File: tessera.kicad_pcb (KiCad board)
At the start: 4 copper layers, 54 x 85.6 mm, 108 parts, among them J1 USB-C, J2 532610271, J3 PinHeader_2x05, Q1 NTK3139P, Q2 NTK3134N, Q3 NTK3134N, SW1 EVQP7A01P, SW2 EVQP7A01P, U1 USBLC6-2P6, U2 BQ25170J, U3 TPS62840DLCR, U4 ISP1807-LR-RS, U5 D3V3XA4B10LP, U6 ST25DV64KC-JF6D3, U7 STSAFA120DFSPL05

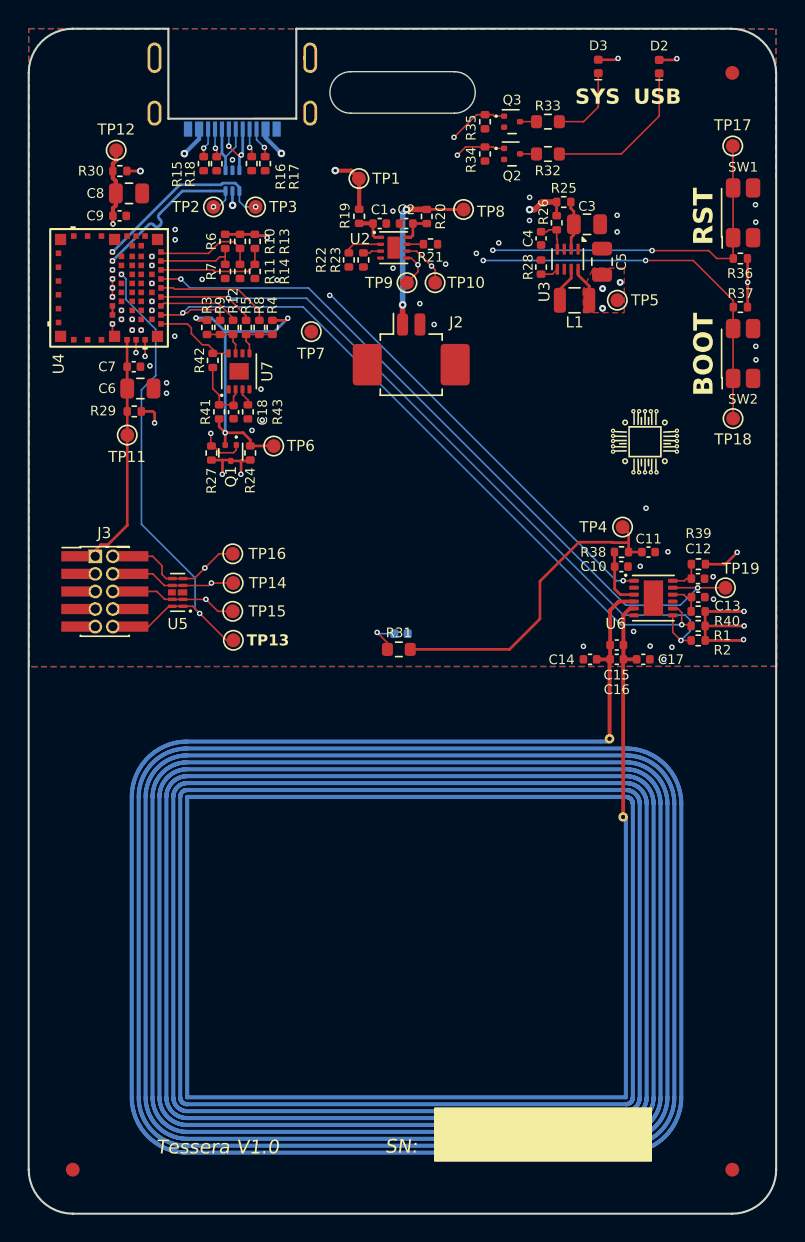
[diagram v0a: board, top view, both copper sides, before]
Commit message: fix(hardware): tighten PCB edge clearance and diff-pair rules, update logo
- Bump lib submodule: assign IPNs to another batch of approved
  capacitor selections
- Update the embedded logo artwork on every schematic sheet to the
  new Logos/logo.png
- Increase min_copper_edge_clearance to 0.5mm and raise net class
  clearance/spacing to match
- Replace the generic outer/inner-layer trace width & spacing rules
  with a dedicated "USB Diff Pair clearance to other nets" rule
  (0.2023mm, excluding intra-pair spacing already governed by the
  netclass diff_pair_gap)
- Add DRC exclusions for pre-existing clearance/copper-edge/solder-
  mask-bridge items surfaced by the tightened edge-clearance rule
- Continue schematic placement and PCB routing/placement
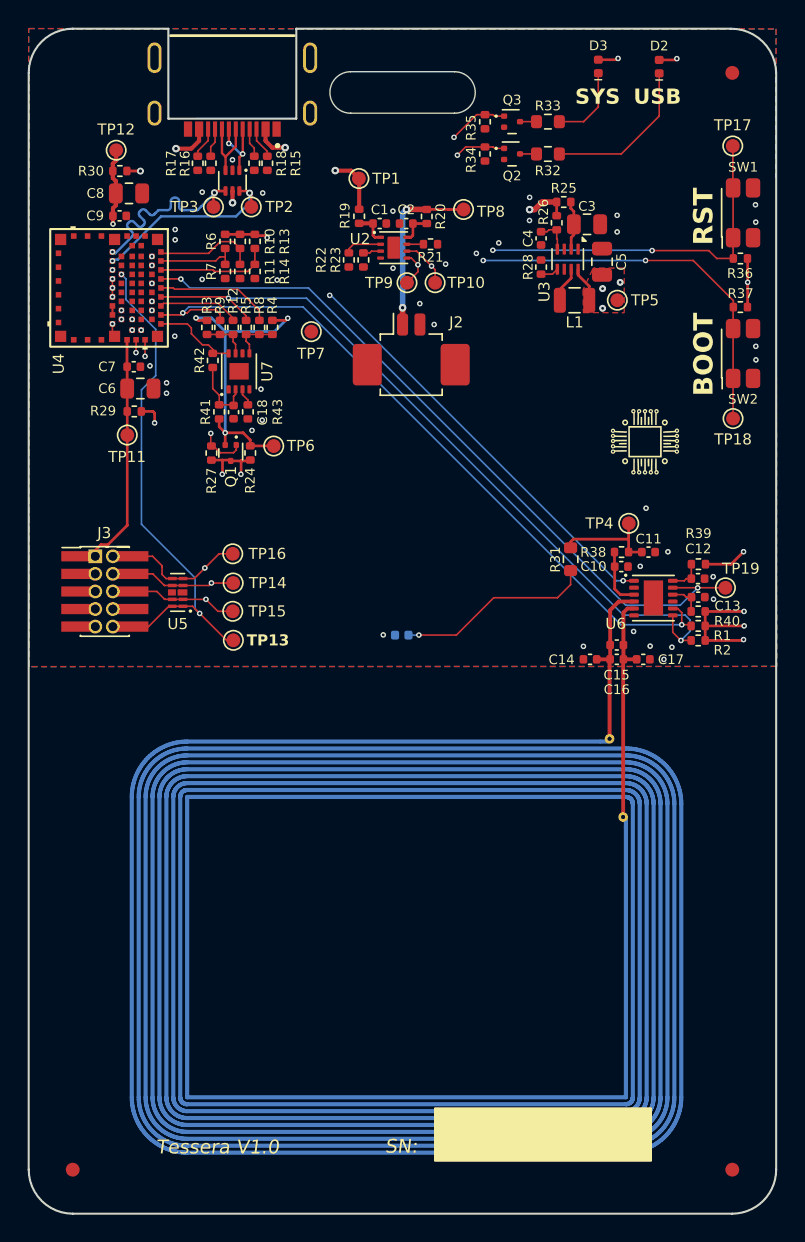
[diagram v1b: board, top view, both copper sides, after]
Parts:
- J1, U1: moved to F.Cu
- moved R31 14.0 mm to (162.2, 88.4), turned to -90 degrees
- moved R17 4.87 mm to (135.3, 59.8)
- moved R15 4.60 mm to (140.3, 59.8)
- moved TP3 3.05 mm to (136.4, 63.0)
- moved R16 2.96 mm to (136.2, 59.8)
- moved TP2 2.74 mm to (139.1, 63.0)
- moved R18 2.72 mm to (139.3, 59.8)
- moved TP4 0.52 mm to (166.4, 85.8)
- moved D1 0.12 mm to (150.0, 93.9), turned to 0 degrees
- turned J1 to 180 degrees
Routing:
- net VCC_EH: track 23.5 -> 7.75 mm
- net Net-(D1-A): track 2.81 -> 14.2 mm
- net /Project Architecture/D-: track 12.7 -> 14.2 mm
- net /Project Architecture/D+: track 13.7 -> 15.1 mm
- net VBUS: track 10.6 -> 11.2 mm
- net Net-(J1-SBU2): track 2.12 -> 2.28 mm, vias 1 -> 0
- net /Project Architecture/USB/USB_D+: track 5.48 -> 5.38 mm, vias 2 -> 0
- net Net-(J1-CC1): track 2.04 -> 2.10 mm, vias 1 -> 0
- net Net-(J1-SBU1): track 2.05 -> 2.09 mm, vias 1 -> 0
- net Net-(J1-CC2): track 2.24 -> 2.27 mm, vias 1 -> 0
- net /Project Architecture/USB/USB_D-: track 5.41 -> 5.43 mm, vias 0 -> 2
- net GND: vias 43 -> 46

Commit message: feat(hardware): add fiducial markers on bottom layer, add via stich and teardrops
- Add FIDUCIAL_D1_0mm_Mask_2_0mm reference marks to Project
  Architecture.kicad_sch and place the corresponding
  Fiducial_1mm_Mask2mm footprints on the PCB (for pick & place
  alignment)
- Added via stiching network
- Added teardrops
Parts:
- added MECH4: FIDUCIAL, Mechanical:Fiducial_1mm_Mask2mm, B.Cu at (126.2, 132.5)
- added MECH5: FIDUCIAL, Mechanical:Fiducial_1mm_Mask2mm, B.Cu at (173.9, 53.3)
- added MECH6: FIDUCIAL, Mechanical:Fiducial_1mm_Mask2mm, B.Cu at (173.9, 132.5)
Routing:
- net VCC: track 164.2 -> 164.1 mm, vias 14 -> 15
- net GND: vias 46 -> 216
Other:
- board text added: "{ "ViaStitching": "0.2", "GND": { "HSpacing": "2.54", "VSpacing": "2.54", "Clearance": "0", "Randomize": false } }"
- board text removed: "{ "ViaStitching": "0.2", "GND": { "HSpacing": "2", "VSpacing": "2", "Clearance": "0", "Randomize": false } }"
